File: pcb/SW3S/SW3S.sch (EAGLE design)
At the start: 52 parts, among them K1 PROG, T1 BC807, T2 BC817, T4 IRL3303, T5 IRL3303

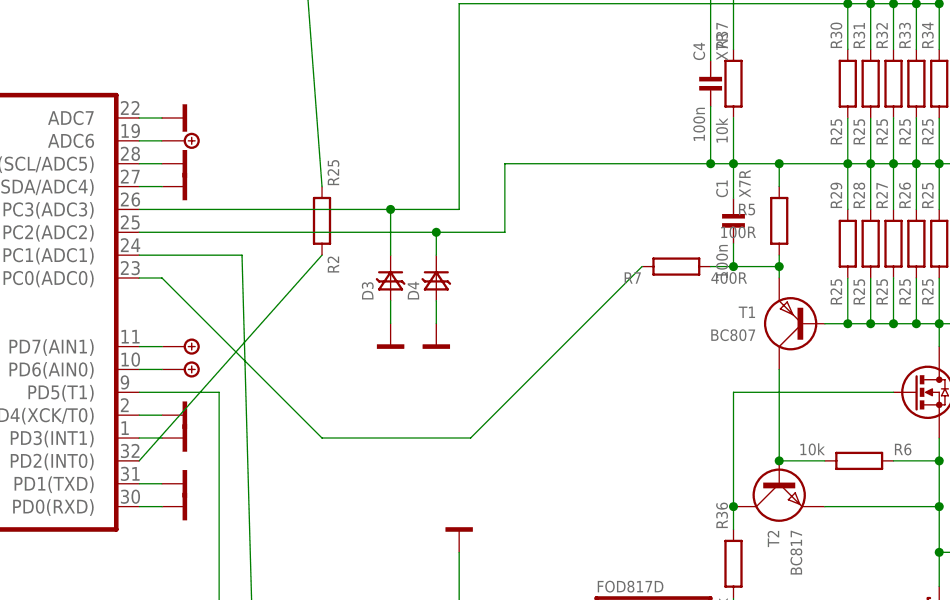
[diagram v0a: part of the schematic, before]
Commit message: Regulace maximalniho nabijeciho proudu neni potreba
V prvni fazi se nabiji baterie konstantnim proudem a v pripade dosazeni U 4.15V/clanek (rezerva 50mV) se nabijeni uplne odpoji.
V pripade kdy balancer nebude stihat vyvazit baterii se tez nabijeni odpoji do okamziku vyvazeni vsech clanku baterie pod mez danou fw.
V pripade podvybiti baterie pod 3V elektronika nepovoli nabijeni (baterii je nutno nabit externi "inteligentni" nabijeckou.

Pozor:

Je potreba nabijet ze zdroje 12-14V kvuli ubytku napeti / ztratovem vykonu na regulacnim tranzistoru.
Ve firmware musi byt odpojeni nabijeni v pripade prehrati CPU nad stanovenou, docela nizkou mez !!! (CPU je blizko regulacniho T)
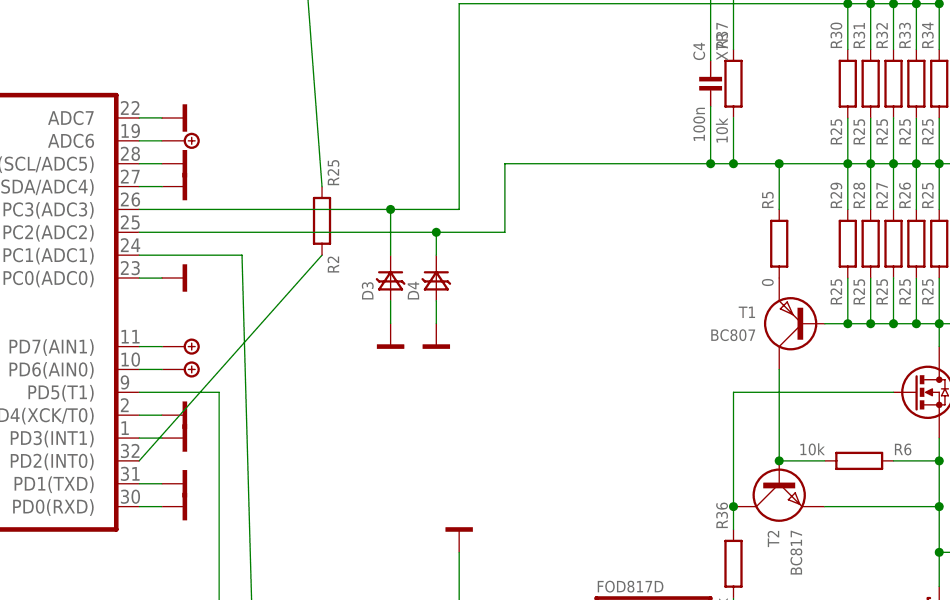
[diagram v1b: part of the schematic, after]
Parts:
- removed C1: 100n, !discrete:C0805
- removed R7: 400R, !discrete:R_R0805
- R5: value 100R -> 0
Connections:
- removed net N$5: IO1A.PC0(ADC0), R7.2
- removed net N$8: C1.2, R5.1, R7.1, T1.E
- new net N$21: R5.1, T1.E
- net BAT-: no longer C1.1
- net GND: now also IO1A.PC0(ADC0)
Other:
- moved on the sheet: R5
